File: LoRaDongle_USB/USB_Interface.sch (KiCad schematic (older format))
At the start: 25 parts

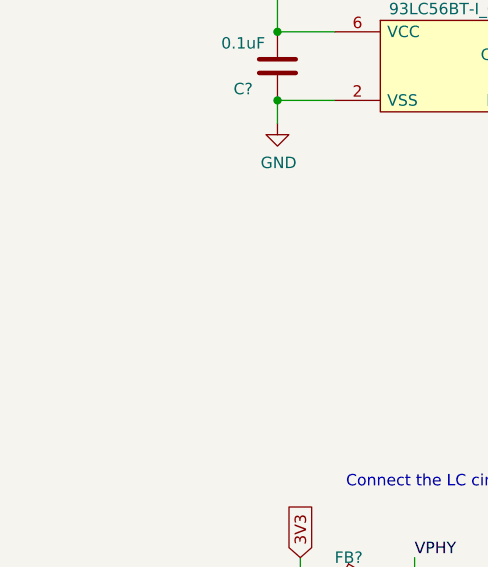
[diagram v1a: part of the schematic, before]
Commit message: updated RF circuitry
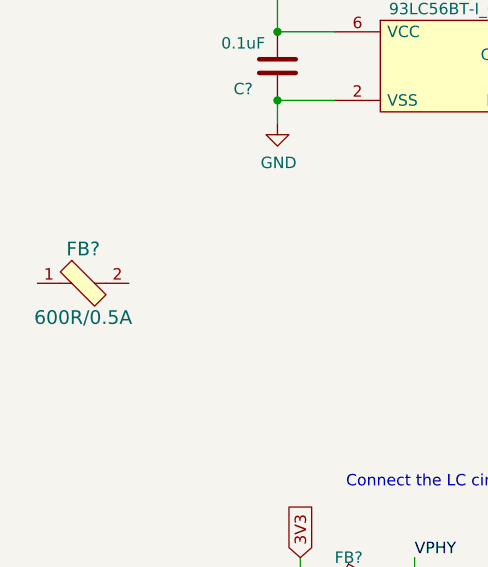
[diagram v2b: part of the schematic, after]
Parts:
- added FB?: 600R/0.5A, digikey-footprints:0603, symbol dk_Ferrite-Beads-and-Chips:BLM18AG601SN1D
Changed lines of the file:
@@
 $Descr A4 11693 8268
 encoding utf-8
-Sheet 6 7
+Sheet 4 7
 Title ""
 Date ""
@@
 Text HLabel 5550 2300 0    50   Input ~ 0
 DP
+$Comp
+L dk_Ferrite-Beads-and-Chips:BLM18AG601SN1D FB?
+U 1 1 615D8A3B
+P 1700 4000
+F 0 "FB?" H 1700 4150 60  0000 C CNN
+F 1 "600R/0.5A" H 1700 3850 60  0000 C CNN
+F 2 "digikey-footprints:0603" H 1900 4200 60  0001 L CNN
+F 3 "https://www.murata.com/en-us/products/productdata/8796738650142/ENFA0003.pdf" H 1900 4300 60  0001 L CNN
+F 4 "490-1014-1-ND" H 1900 4400 60  0001 L CNN "Digi-Key_PN"
+F 5 "BLM18AG601SN1D" H 1900 4500 60  0001 L CNN "MPN"
+F 6 "Filters" H 1900 4600 60  0001 L CNN "Category"
+F 7 "Ferrite Beads and Chips" H 1900 4700 60  0001 L CNN "Family"
+F 8 "https://www.murata.com/en-us/products/productdata/8796738650142/ENFA0003.pdf" H 1900 4800 60  0001 L CNN "DK_Datasheet_Link"
+F 9 "/product-detail/en/murata-electronics-north-america/BLM18AG601SN1D/490-1014-1-ND/584462" H 1900 4900 60  0001 L CNN "DK_Detail_Page"
+F 10 "FERRITE BEAD 600 OHM 0603 1LN" H 1900 5000 60  0001 L CNN "Description"
+F 11 "Murata Electronics North America" H 1900 5100 60  0001 L CNN "Manufacturer"
+F 12 "Active" H 1900 5200 60  0001 L CNN "Status"
+	1    1700 4000
+	1    0    0    -1
+$EndComp
 $EndSCHEMATC

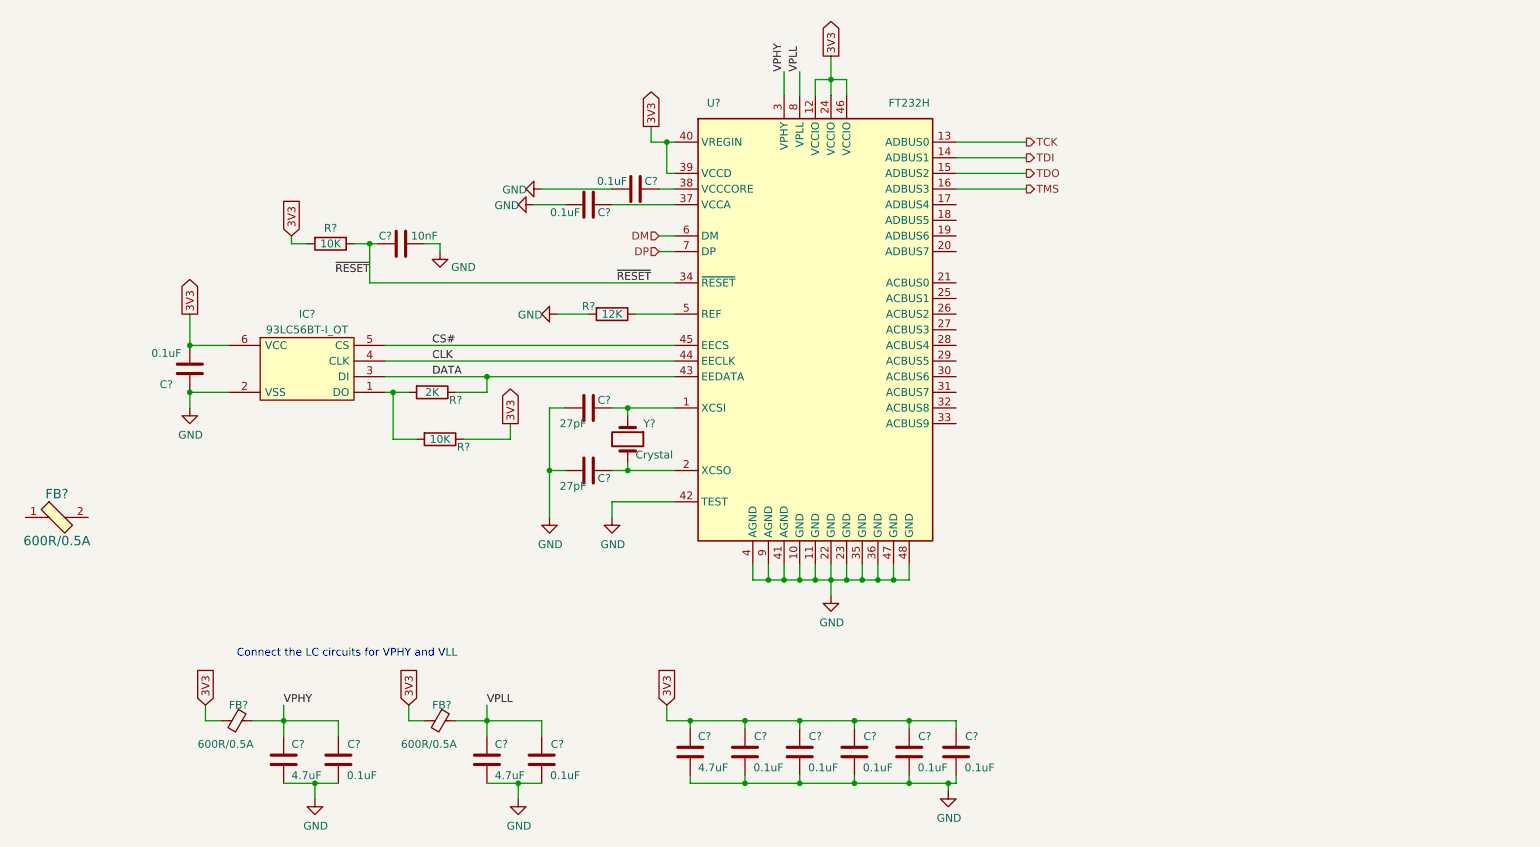
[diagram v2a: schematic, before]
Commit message: updated with dip switch
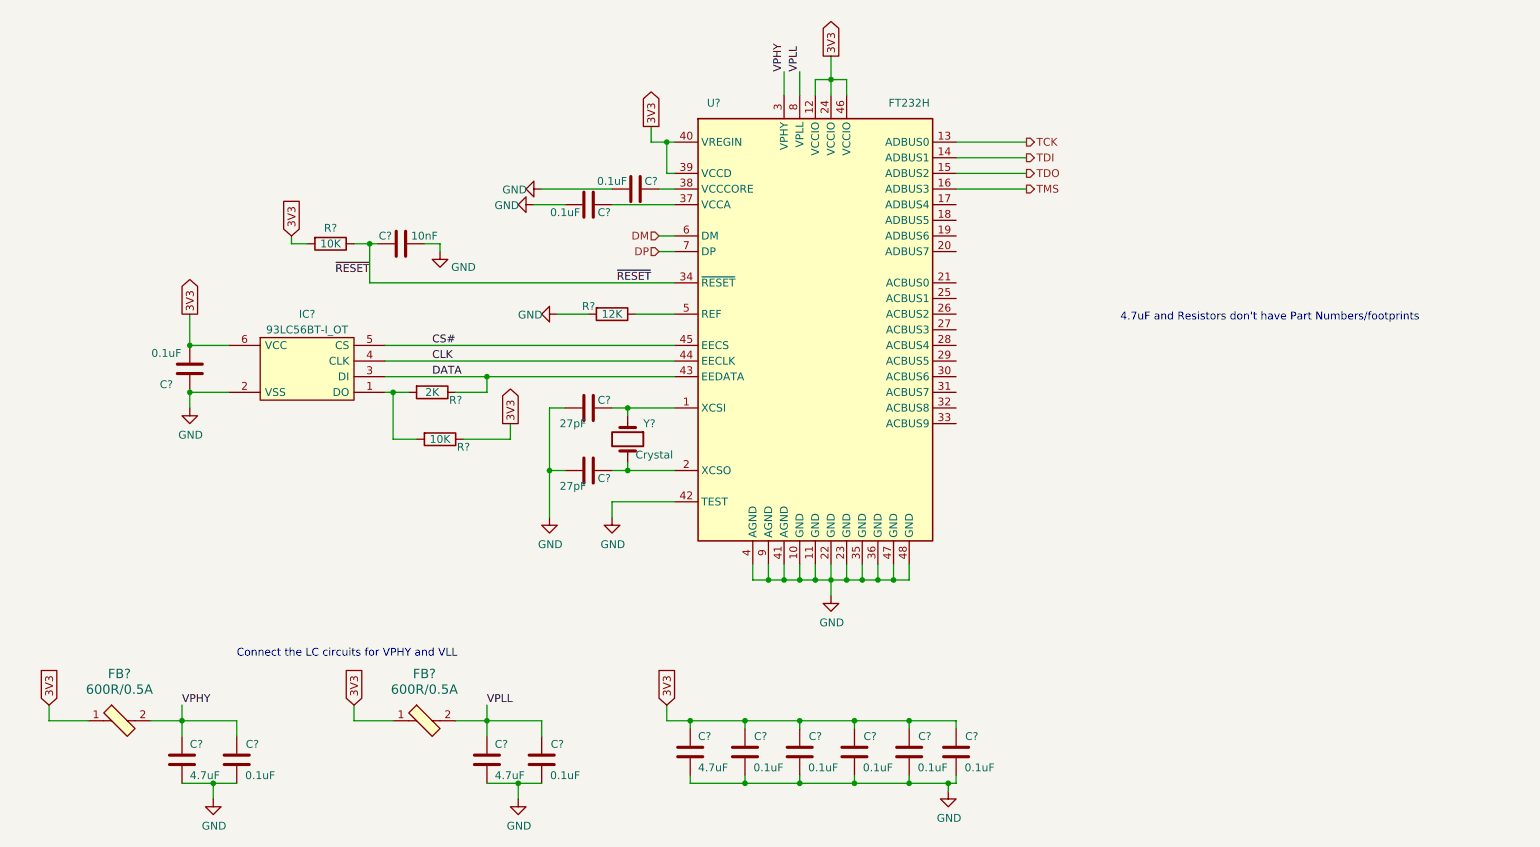
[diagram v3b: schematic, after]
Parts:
- removed FB? (x2): 600R/0.5A, digikey-footprints:0603, symbol Device:Ferrite_Bead_Small
- added FB?: 600R/0.5A, digikey-footprints:0603, symbol dk_Ferrite-Beads-and-Chips:BLM18AG601SN1D
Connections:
- net 3V3: now also FB?.1, FB?.1
- net VPHY: now also FB?.2
- net VPLL: now also FB?.2
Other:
- note added: "4.7uF and Resistors don't have Part Numbers/footprints"
- moved on the sheet: C?, FB?
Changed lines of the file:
@@
 $Descr A4 11693 8268
 encoding utf-8
-Sheet 4 7
+Sheet 5 7
 Title ""
 Date ""
@@
 Text Notes 2850 4900 0    50   ~ 0
 Connect the LC circuits for VPHY and VLL
-Text GLabel 2650 5200 1    50   Input ~ 0
+Text GLabel 1650 5200 1    50   Input ~ 0
 3V3
 $Comp
-L Device:Ferrite_Bead_Small FB?
-U 1 1 6191A257
-P 2850 5300
-AR Path="/6191A257" Ref="FB?"  Part="1"
-AR Path="/618AACD4/6191A257" Ref="FB?"  Part="1"
-F 0 "FB?" V 2750 5250 50  0000 L CNN
-F 1 "600R/0.5A" V 3000 5050 50  0000 L CNN
-F 2 "digikey-footprints:0603" V 2780 5300 50  0001 C CNN
-F 3 "~" H 2850 5300 50  0001 C CNN
-F 4 "742863160" H 2850 5300 50  0001 C CNN "Part Number"
-	1    2850 5300
-	0    1    1    0
-$EndComp
-$Comp
 L Device:C C?
 U 1 1 6191A25D
-P 3150 5550
+P 2500 5550
 AR Path="/6191A25D" Ref="C?"  Part="1"
 AR Path="/618AACD4/6191A25D" Ref="C?"  Part="1"
-F 0 "C?" H 3200 5650 50  0000 L CNN
-F 1 "4.7uF" H 3200 5450 50  0000 L CNN
-F 2 "Capacitor_SMD:C_0603_1608Metric" H 3188 5400 50  0001 C CNN
-F 3 "~" H 3150 5550 50  0001 C CNN
-	1    3150 5550
+F 0 "C?" H 2550 5650 50  0000 L CNN
+F 1 "4.7uF" H 2550 5450 50  0000 L CNN
+F 2 "Capacitor_SMD:C_0603_1608Metric" H 2538 5400 50  0001 C CNN
+F 3 "~" H 2500 5550 50  0001 C CNN
+	1    2500 5550
 	1    0    0    -1
 $EndComp
@@
 L power:GND #PWR?
 U 1 1 6191A263
-P 3350 5800
+P 2700 5800
 AR Path="/6191A263" Ref="#PWR?"  Part="1"
 AR Path="/618AACD4/6191A263" Ref="#PWR?"  Part="1"
-F 0 "#PWR?" H 3350 5550 50  0001 C CNN
-F 1 "GND" H 3355 5627 50  0000 C CNN
-F 2 "" H 3350 5800 50  0001 C CNN
-F 3 "" H 3350 5800 50  0001 C CNN
-	1    3350 5800
-	1    0    0    -1
-$EndComp
-Wire Wire Line
-	2650 5200 2650 5300
-Wire Wire Line
-	2650 5300 2750 5300
-Wire Wire Line
-	2950 5300 3150 5300
-Wire Wire Line
-	3150 5300 3150 5400
-Wire Wire Line
-	3150 5700 3350 5700
-Wire Wire Line
-	3350 5700 3350 5800
-Wire Wire Line
-	3500 5700 3350 5700
-Connection ~ 3350 5700
-Wire Wire Line
-	3500 5400 3500 5300
-Wire Wire Line
-	3500 5300 3150 5300
-Connection ~ 3150 5300
-Wire Wire Line
-	3150 5300 3150 5200
-Text GLabel 3950 5200 1    50   Input ~ 0
+F 0 "#PWR?" H 2700 5550 50  0001 C CNN
+F 1 "GND" H 2705 5627 50  0000 C CNN
+F 2 "" H 2700 5800 50  0001 C CNN
+F 3 "" H 2700 5800 50  0001 C CNN
+	1    2700 5800
+	1    0    0    -1
+$EndComp
+Wire Wire Line
+	1650 5200 1650 5300
+Wire Wire Line
+	2300 5300 2500 5300
+Wire Wire Line
+	2500 5300 2500 5400
+Wire Wire Line
+	2500 5700 2700 5700
+Wire Wire Line
+	2700 5700 2700 5800
+Wire Wire Line
+	2850 5700 2700 5700
+Connection ~ 2700 5700
+Wire Wire Line
+	2850 5400 2850 5300
+Wire Wire Line
+	2850 5300 2500 5300
+Connection ~ 2500 5300
+Wire Wire Line
+	2500 5300 2500 5200
+Text GLabel 3600 5200 1    50   Input ~ 0
 3V3
-$Comp
-L Device:Ferrite_Bead_Small FB?
-U 1 1 6191A277
-P 4150 5300
-AR Path="/6191A277" Ref="FB?"  Part="1"
-AR Path="/618AACD4/6191A277" Ref="FB?"  Part="1"
-F 0 "FB?" V 4050 5250 50  0000 L CNN
-F 1 "600R/0.5A" V 4300 5050 50  0000 L CNN
-F 2 "digikey-footprints:0603" V 4080 5300 50  0001 C CNN
-F 3 "~" H 4150 5300 50  0001 C CNN
-F 4 "742863160" H 4150 5300 50  0001 C CNN "Part Number"
-	1    4150 5300
-	0    1    1    0
-$EndComp
 $Comp
 L Device:C C?
@@
 $EndComp
 Wire Wire Line
-	3950 5200 3950 5300
-Wire Wire Line
-	3950 5300 4050 5300
+	3600 5200 3600 5300
 Wire Wire Line
 	4250 5300 4450 5300
@@
 Wire Wire Line
 	4450 5300 4450 5200
-Text Label 3150 5200 0    50   ~ 0
+Text Label 2500 5200 0    50   ~ 0
 VPHY
 Text Label 4450 5200 0    50   ~ 0
@@
 L Device:C C?
 U 1 1 6191A2B6
-P 3500 5550
+P 2850 5550
 AR Path="/6191A2B6" Ref="C?"  Part="1"
 AR Path="/618AACD4/6191A2B6" Ref="C?"  Part="1"
-F 0 "C?" H 3400 5450 50  0000 C CNN
-F 1 "0.1uF" H 3350 5650 50  0000 C CNN
-F 2 "Capacitor_SMD:C_0402_1005Metric" H 3538 5400 50  0001 C CNN
-F 3 "~" H 3500 5550 50  0001 C CNN
-F 4 "GCM155R71C104KA55J" V 3500 5550 50  0001 C CNN "Part Number"
-	1    3500 5550
+F 0 "C?" H 2750 5450 50  0000 C CNN
+F 1 "0.1uF" H 2700 5650 50  0000 C CNN
+F 2 "Capacitor_SMD:C_0402_1005Metric" H 2888 5400 50  0001 C CNN
+F 3 "~" H 2850 5550 50  0001 C CNN
+F 4 "GCM155R71C104KA55J" V 2850 5550 50  0001 C CNN "Part Number"
+	1    2850 5550
 	-1   0    0    1
 $EndComp
@@
 F 4 "GCM155R71C104KA55J" V 4800 5550 50  0001 C CNN "Part Number"
 	1    4800 5550
-	-1   0    0    1
-$EndComp
-$Comp
-L Device:C C?
-U 1 1 6191A2C4
-P 6100 5500
-AR Path="/6191A2C4" Ref="C?"  Part="1"
-AR Path="/618AACD4/6191A2C4" Ref="C?"  Part="1"
-F 0 "C?" H 6000 5400 50  0000 C CNN
-F 1 "0.1uF" H 5950 5600 50  0000 C CNN
-F 2 "Capacitor_SMD:C_0402_1005Metric" H 6138 5350 50  0001 C CNN
-F 3 "~" H 6100 5500 50  0001 C CNN
-F 4 "GCM155R71C104KA55J" V 6100 5500 50  0001 C CNN "Part Number"
-	1    6100 5500
 	-1   0    0    1
 $EndComp
@@
 L dk_Ferrite-Beads-and-Chips:BLM18AG601SN1D FB?
 U 1 1 615D8A3B
-P 1700 4000
-F 0 "FB?" H 1700 4150 60  0000 C CNN
-F 1 "600R/0.5A" H 1700 3850 60  0000 C CNN
-F 2 "digikey-footprints:0603" H 1900 4200 60  0001 L CNN
-F 3 "https://www.murata.com/en-us/products/productdata/8796738650142/ENFA0003.pdf" H 1900 4300 60  0001 L CNN
-F 4 "490-1014-1-ND" H 1900 4400 60  0001 L CNN "Digi-Key_PN"
-F 5 "BLM18AG601SN1D" H 1900 4500 60  0001 L CNN "MPN"
-F 6 "Filters" H 1900 4600 60  0001 L CNN "Category"
-F 7 "Ferrite Beads and Chips" H 1900 4700 60  0001 L CNN "Family"
-F 8 "https://www.murata.com/en-us/products/productdata/8796738650142/ENFA0003.pdf" H 1900 4800 60  0001 L CNN "DK_Datasheet_Link"
-F 9 "/product-detail/en/murata-electronics-north-america/BLM18AG601SN1D/490-1014-1-ND/584462" H 1900 4900 60  0001 L CNN "DK_Detail_Page"
-F 10 "FERRITE BEAD 600 OHM 0603 1LN" H 1900 5000 60  0001 L CNN "Description"
-F 11 "Murata Electronics North America" H 1900 5100 60  0001 L CNN "Manufacturer"
-F 12 "Active" H 1900 5200 60  0001 L CNN "Status"
-	1    1700 4000
-	1    0    0    -1
-$EndComp
+P 2100 5300
+F 0 "FB?" H 2100 5600 60  0000 C CNN
+F 1 "600R/0.5A" H 2100 5500 60  0000 C CNN
+F 2 "digikey-footprints:0603" H 2300 5500 60  0001 L CNN
+F 3 "https://www.murata.com/en-us/products/productdata/8796738650142/ENFA0003.pdf" H 2300 5600 60  0001 L CNN
+F 4 "490-1014-1-ND" H 2300 5700 60  0001 L CNN "Digi-Key_PN"
+F 5 "BLM18AG601SN1D" H 2300 5800 60  0001 L CNN "MPN"
+F 6 "Filters" H 2300 5900 60  0001 L CNN "Category"
+F 7 "Ferrite Beads and Chips" H 2300 6000 60  0001 L CNN "Family"
+F 8 "https://www.murata.com/en-us/products/productdata/8796738650142/ENFA0003.pdf" H 2300 6100 60  0001 L CNN "DK_Datasheet_Link"
+F 9 "/product-detail/en/murata-electronics-north-america/BLM18AG601SN1D/490-1014-1-ND/584462" H 2300 6200 60  0001 L CNN "DK_Detail_Page"
+F 10 "FERRITE BEAD 600 OHM 0603 1LN" H 2300 6300 60  0001 L CNN "Description"
+F 11 "Murata Electronics North America" H 2300 6400 60  0001 L CNN "Manufacturer"
+F 12 "Active" H 2300 6500 60  0001 L CNN "Status"
+	1    2100 5300
+	1    0    0    -1
+$EndComp
+Wire Wire Line
+	1650 5300 1900 5300
+$Comp
+L dk_Ferrite-Beads-and-Chips:BLM18AG601SN1D FB?
+U 1 1 616966EF
+P 4050 5300
+F 0 "FB?" H 4050 5600 60  0000 C CNN
+F 1 "600R/0.5A" H 4050 5500 60  0000 C CNN
+F 2 "digikey-footprints:0603" H 4250 5500 60  0001 L CNN
+F 3 "https://www.murata.com/en-us/products/productdata/8796738650142/ENFA0003.pdf" H 4250 5600 60  0001 L CNN
+F 4 "490-1014-1-ND" H 4250 5700 60  0001 L CNN "Digi-Key_PN"
+F 5 "BLM18AG601SN1D" H 4250 5800 60  0001 L CNN "MPN"
+F 6 "Filters" H 4250 5900 60  0001 L CNN "Category"
+F 7 "Ferrite Beads and Chips" H 4250 6000 60  0001 L CNN "Family"
+F 8 "https://www.murata.com/en-us/products/productdata/8796738650142/ENFA0003.pdf" H 4250 6100 60  0001 L CNN "DK_Datasheet_Link"
+F 9 "/product-detail/en/murata-electronics-north-america/BLM18AG601SN1D/490-1014-1-ND/584462" H 4250 6200 60  0001 L CNN "DK_Detail_Page"
+F 10 "FERRITE BEAD 600 OHM 0603 1LN" H 4250 6300 60  0001 L CNN "Description"
+F 11 "Murata Electronics North America" H 4250 6400 60  0001 L CNN "Manufacturer"
+F 12 "Active" H 4250 6500 60  0001 L CNN "Status"
+	1    4050 5300
+	1    0    0    -1
+$EndComp
+Wire Wire Line
+	3600 5300 3850 5300
+$Comp
+L Device:C C?
+U 1 1 6191A2C4
+P 6100 5500
+AR Path="/6191A2C4" Ref="C?"  Part="1"
+AR Path="/618AACD4/6191A2C4" Ref="C?"  Part="1"
+F 0 "C?" H 6000 5400 50  0000 C CNN
+F 1 "0.1uF" H 5950 5600 50  0000 C CNN
+F 2 "Capacitor_SMD:C_0402_1005Metric" H 6138 5350 50  0001 C CNN
+F 3 "~" H 6100 5500 50  0001 C CNN
+F 4 "GCM155R71C104KA55J" V 6100 5500 50  0001 C CNN "Part Number"
+	1    6100 5500
+	-1   0    0    1
+$EndComp
+Text Notes 8500 2750 0    50   ~ 0
+4.7uF and Resistors don't have Part Numbers/footprints
 $EndSCHEMATC
